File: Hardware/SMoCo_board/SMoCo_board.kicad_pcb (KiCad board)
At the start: 2 copper layers, 78 parts, among them J1 Conn_01x02, J2 Conn_01x02, J3 Conn_01x03, J5 Conn_01x06, J6 Conn_01x02, J7 Conn_01x04, J8 Conn_01x02, Q1 BSS138, Q2 AO3401A, Q3 BSS138, Q4 AO3401A, Q5 BSS138, Q6 AO3401A, U2 VNH7040AYTR, U3 SN65HVD232, U4 AP63203WU, U5 STM32F072C8Tx

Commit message: rewind
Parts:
- C1, C10, C11, C12, C13, C14, C9, J1, J2, Q6, R14, R15, R17, R18, R19, R7, R9, U2: moved to B.Cu
- R20, R21: footprint Resistor_THT:R_Array_SIP4 -> Resistor_SMD:R_0603_1608Metric_Pad0.98x0.95mm_HandSolder
- R22, R23, R24: footprint Resistor_THT:R_Array_SIP4 -> Resistor_SMD:R_0603_1608Metric_Pad0.98x0.95mm_HandSolder; moved to B.Cu
- moved TP1 166.0 mm to (222.1, 148.1)
- moved L1 162.5 mm to (228.5, 146.6)
- moved C5 162.1 mm to (221.2, 151.9), turned to 180 degrees
- moved C4 162.0 mm to (228.5, 151.6), turned to 90 degrees
- moved D2 161.8 mm to (228.5, 141.7), turned to 180 degrees
- moved C8 159.4 mm to (221.2, 150.4), turned to 180 degrees
- moved U4 157.3 mm to (225.7, 152.1), turned to 0 degrees
- moved C19 151.1 mm to (221.2, 155.1), turned to 180 degrees
- moved C6 148.7 mm to (221.2, 153.6), turned to 180 degrees
- moved R4 116.3 mm to (162.0, 181.2), turned to 90 degrees
- moved J5 116.2 mm to (188.8, 155.6), turned to 90 degrees
- moved R8 114.4 mm to (160.5, 181.2), turned to 90 degrees
- moved R6 113.4 mm to (159.0, 181.2), turned to 90 degrees
- moved J7 105.8 mm to (170.7, 168.7)
- moved MOSFET1 104.6 mm to (153.7, 129.7)
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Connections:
- R15 pad 2: /Untitled Sheet/Led_B_Out -> /Led_B_Out
- R18 pad 2: /Untitled Sheet/Led_G_Out -> /Led_G_Out
- R21 pad 2: /Untitled Sheet/Led_R_Out -> /Led_R_Out
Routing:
- net +24V: track 0.00 -> 21.5 mm
- net V_AUX: track 0.00 -> 21.1 mm
- net +3.3V: track 0.00 -> 11.7 mm
- net /LIM A: track 0.00 -> 10.8 mm
- net /LIM B: track 0.00 -> 10.4 mm
- net /NRST: track 0.00 -> 7.86 mm
- net /boot: track 0.00 -> 6.61 mm
- net Net-(MOSFET1-G): track 0.00 -> 6.60 mm
- net /SWDCLK: track 0.00 -> 6.33 mm
- net /SWDIO: track 0.00 -> 5.45 mm
- net Net-(U2-MultiSense): track 0.00 -> 5.27 mm
- net Net-(U5-PA3): track 0.00 -> 3.72 mm
- net Net-(U5-PA2): track 0.00 -> 3.71 mm
- net Net-(U4-BST): track 0.00 -> 3.59 mm
- net Net-(U5-PA7): track 0.00 -> 3.37 mm
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
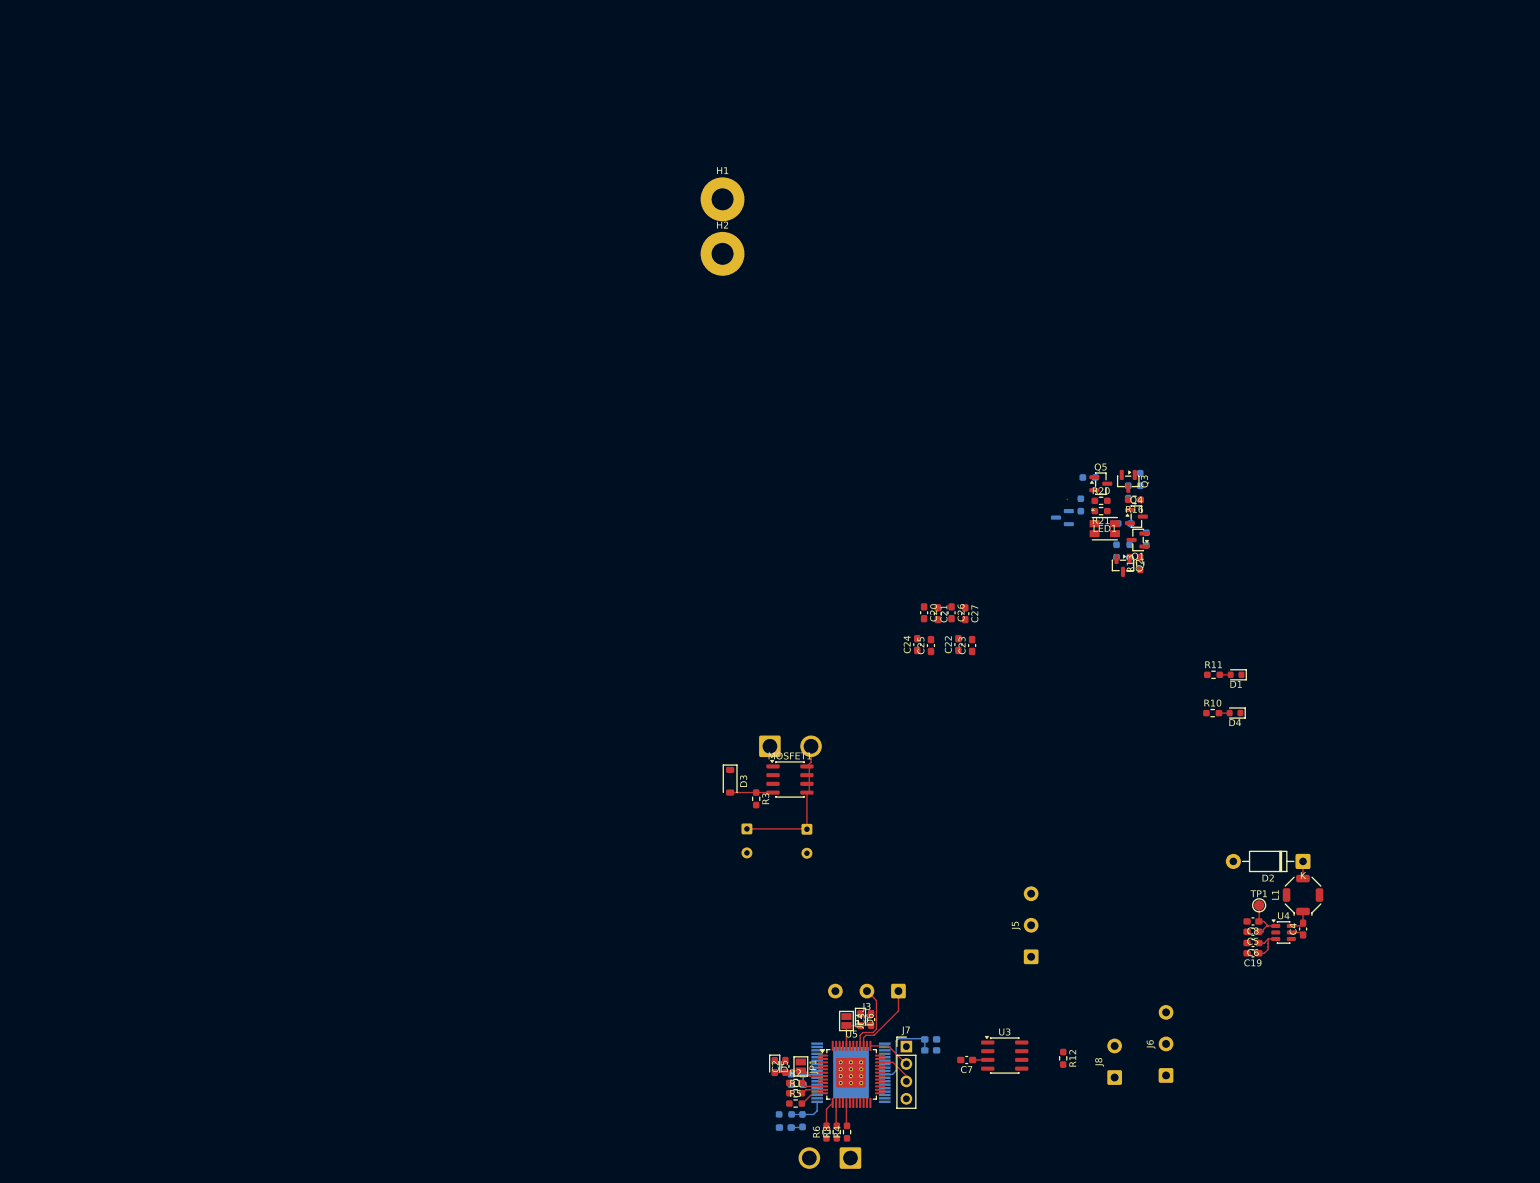
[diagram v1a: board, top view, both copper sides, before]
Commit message: Board Size
Board size should be final and more mouse bites
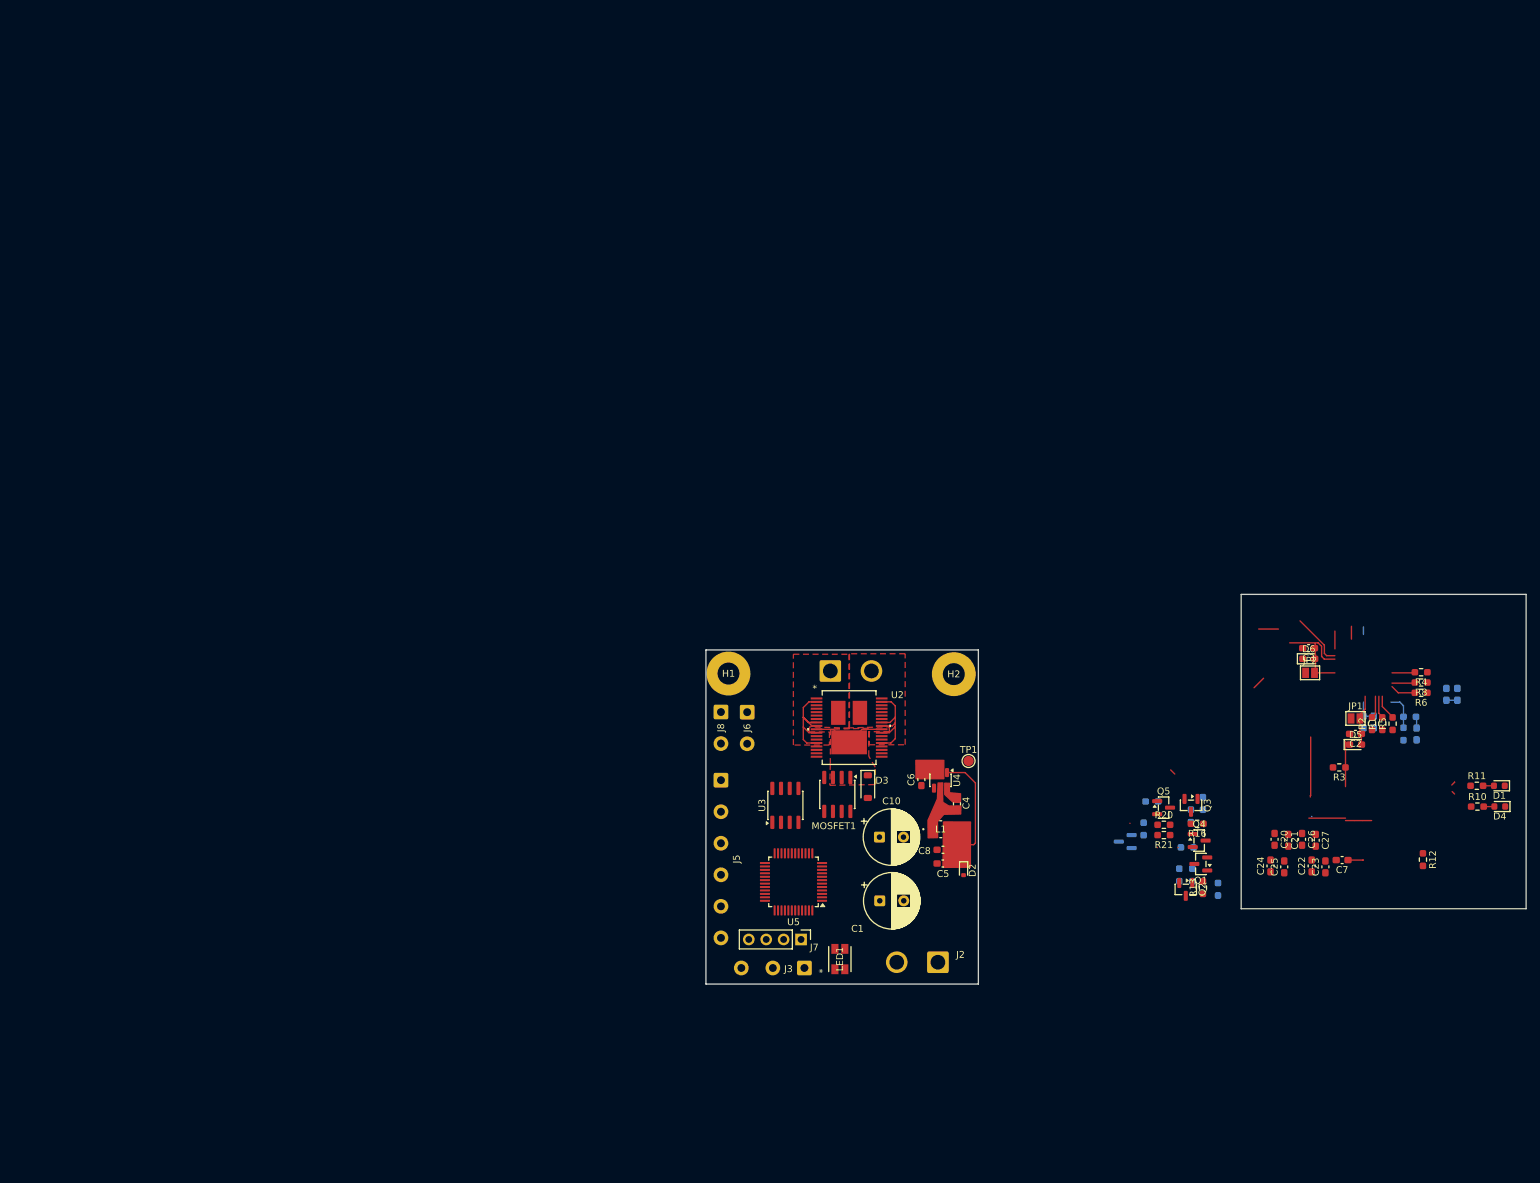
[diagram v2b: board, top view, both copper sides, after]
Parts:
- removed C19: 47uF, Capacitor_SMD:C_0603_1608Metric_Pad1.08x0.95mm_HandSolder
- C1, C10, J2: moved to F.Cu
- D2: value D_Zener -> MMSZ4685-TP; footprint Diode_THT:D_DO-41_SOD81_P10.16mm_Horizontal -> Diode_SMD:D_SOD-523
- J5: footprint Connector_Wire:SolderWire-0.5sqmm_1x03_P4.6mm_D0.9mm_OD2.1mm -> Connector_Wire:SolderWire-0.5sqmm_1x06_P4.6mm_D0.9mm_OD2.1mm
- J6: footprint Connector_Wire:SolderWire-0.5sqmm_1x03_P4.6mm_D0.9mm_OD2.1mm -> Connector_Wire:SolderWire-0.5sqmm_1x02_P4.6mm_D0.9mm_OD2.1mm
- L1: footprint Inductor_SMD:L_Bourns_SRU5016_5.2x5.2mm -> Inductor:IND_TFM252012ALMA1R0MTAA_TDK
- LED1: footprint footprints:PLCC4_3p5x2p8_SLD -> RGBLED:PLCC4_3p5x2p8_SLD
- U2: footprint Package_SO:ST_PowerSSO-36_SlugDown_ThermalVias -> VNH7040AYTR:POWERSSO-36TP_STM; moved to F.Cu
- moved C9 108.5 mm to (245.1, 123.1), turned to -90 degrees
- moved R6 107.8 mm to (245.7, 117.1), turned to 180 degrees
- moved R8 107.5 mm to (245.7, 115.6), turned to 180 degrees
- moved R4 107.3 mm to (245.7, 114.1), turned to 180 degrees
- moved R7 106.4 mm to (244.1, 120.6), turned to 180 degrees
- moved R9 105.9 mm to (243.1, 123.1), turned to -90 degrees
- moved R5 103.2 mm to (241.6, 121.6), turned to 90 degrees
- moved R1 101.1 mm to (240.1, 121.6), turned to 90 degrees
- moved C12 99.3 mm to (238.8, 121.4), turned to 90 degrees
- moved R2 99.1 mm to (238.6, 121.6), turned to 90 degrees
- moved C11 97.3 mm to (237.3, 121.4), turned to 90 degrees
- moved D5 96.9 mm to (236.2, 124.6), turned to 0 degrees
- moved C2 96.3 mm to (236.1, 123.1), turned to 180 degrees
- moved JP1 95.5 mm to (236.1, 120.8), turned to 0 degrees
- moved C14 92.7 mm to (251.0, 117.3), turned to -90 degrees
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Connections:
- R15 pad 2: /Led_B_Out -> /Untitled Sheet/Led_B_Out
- R18 pad 2: /Led_G_Out -> /Untitled Sheet/Led_G_Out
- R21 pad 2: /Led_R_Out -> /Untitled Sheet/Led_R_Out
- U2 pad 37: unconnected-(U2-Pad37)_1 -> +24V
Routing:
- net /MOTOR PWR A: track 0.00 -> 16.0 mm
- net /MOTOR PWR B: track 0.07 -> 16.0 mm
- net /boot: track 6.61 -> 15.1 mm
- net /LIM B: track 10.4 -> 1.96 mm
- net +3.3V: track 11.7 -> 18.6 mm
- net +24V: track 21.5 -> 17.5 mm
- net /SWDCLK: track 6.33 -> 2.60 mm
- net /SWDIO: track 5.45 -> 1.88 mm
- net Net-(U4-BST): track 3.59 -> 0.60 mm
- net /LIM A: track 10.8 -> 7.90 mm
- net GND: track 0.07 -> 2.97 mm
- net V_AUX: track 21.1 -> 18.8 mm
- net Net-(U4-SW): track 1.86 -> 0.51 mm
- added copper zone on F.Cu, net +24V
- added copper zone on F.Cu, net /MOTOR PWR A
- added copper zone on F.Cu, net /MOTOR PWR B
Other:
- board outline added: 119.6 x 56.8 mm
